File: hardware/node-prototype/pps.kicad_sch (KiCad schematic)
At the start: 5 parts, among them J5 Conn_Coaxial, Q4 2N7002, Q5 AO3401A

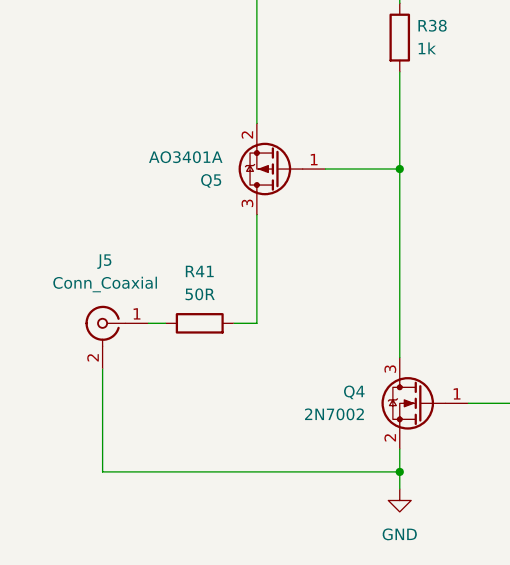
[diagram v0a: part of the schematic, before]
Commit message: Assign footprints
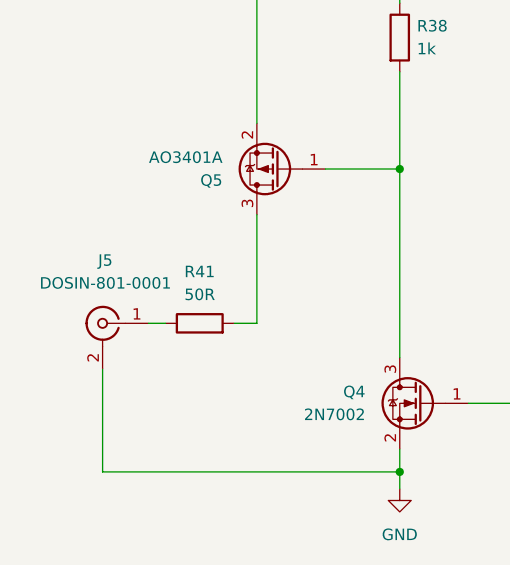
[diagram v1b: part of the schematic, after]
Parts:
- J5: value Conn_Coaxial -> DOSIN-801-0001; footprint (none) -> MYBSP01201ABF_MYBSP00502ABF:DOSIN-801-0001
- R38, R41: footprint (none) -> Resistor_SMD:R_0603_1608Metric
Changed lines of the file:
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@@
       (effects (font (size 1.27 1.27)) (justify left))
     )
-    (property "Footprint" "" (at 160.147 61.595 90)
+    (property "Footprint" "Resistor_SMD:R_0603_1608Metric" (at 160.147 61.595 90)
       (effects (font (size 1.27 1.27)) hide)
     )
@@
       (effects (font (size 1.27 1.27)))
     )
-    (property "Value" "Conn_Coaxial" (at 129.2224 88.9 0)
+    (property "Value" "DOSIN-801-0001" (at 129.2224 88.9 0)
       (effects (font (size 1.27 1.27)))
     )
-    (property "Footprint" "" (at 128.905 93.345 0)
+    (property "Footprint" "MYBSP01201ABF_MYBSP00502ABF:DOSIN-801-0001" (at 128.905 93.345 0)
       (effects (font (size 1.27 1.27)) hide)
     )
-    (property "Datasheet" " ~" (at 128.905 93.345 0)
+    (property "Datasheet" "https://datasheet.lcsc.com/lcsc/2005150732_dosinconn-DOSIN-801-0001_C521212.pdf" (at 128.905 93.345 0)
       (effects (font (size 1.27 1.27)) hide)
     )
@@
       (effects (font (size 1.27 1.27)))
     )
-    (property "Footprint" "" (at 139.7 95.123 90)
+    (property "Footprint" "Resistor_SMD:R_0603_1608Metric" (at 139.7 95.123 90)
       (effects (font (size 1.27 1.27)) hide)
     )

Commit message: Double check schematic
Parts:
- added C35: 1uF, Capacitor_SMD:C_0603_1608Metric, symbol Device:C
- added C47: 100nF, Capacitor_SMD:C_0603_1608Metric, symbol Device:C
- added J6: Conn_01x03, Connector_PinHeader_2.54mm:PinHeader_1x03_P2.54mm_Vertical, symbol Connector_Generic:Conn_01x03
- added JP1: Jumper_2_Open, Jumper:SolderJumper-2_P1.3mm_Open_TrianglePad1.0x1.5mm, symbol Jumper:Jumper_2_Open
- added R47, R51, R52: 100R, Resistor_SMD:R_1206_3216Metric, symbol Device:R
- added R48: 100K, Resistor_SMD:R_0603_1608Metric, symbol Device:R
- added R53: 330K, Resistor_SMD:R_0603_1608Metric, symbol Device:R
- added R54: 47K, Resistor_SMD:R_0603_1608Metric, symbol Device:R
- added R55: 91K, Resistor_SMD:R_0603_1608Metric, symbol Device:R
- added R56: 620K, Resistor_SMD:R_0603_1608Metric, symbol Device:R
- added TP1, TP2 (x2): TestPoint, TestPoint:TestPoint_Pad_D2.0mm, symbol Connector:TestPoint
- added U4: SRV05-4, Package_TO_SOT_SMD:SOT-23-6, symbol Power_Protection:SRV05-4
- R41: value 50R -> 100R; footprint Resistor_SMD:R_0603_1608Metric -> Resistor_SMD:R_1206_3216Metric
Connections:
- net GND: now also C35.2, C47.2, J6.3 (Pin_3), JP1.1 (A), R48.2, R51.1, R52.1, R55.2, R56.2, U4.2 (VN)
- net PPS_OUT: now also TP1.1
- net PPS_BNC: now reaches J5.1 (In), R41.1
- net PPS_BNC: now also R47.1, R48.1, U4.1 (IO1)
- net at Q5.3 (D), R41.2: now also R47.2
- net VDD renamed +5V
- net +5V: now also C35.1, C47.1, U4.5 (VP)
- new net SYNC_IN0: R53.2, R56.1, TP2.1
- new net SYNC_IN1: JP1.2 (B), R54.2, R55.1, TP2.1
- new net SYNC_IN_1M: J6.1 (Pin_1), R53.1, U4.3 (IO2)
- new net SYNC_IN_50R: J6.2 (Pin_2), R51.2, R52.2, R54.1, U4.4 (IO3)
- no-connect marks 0 -> 1
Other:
- moved on the sheet: J5, Q4, Q5, R38, R41

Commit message: Finish placement
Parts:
- added J7: ~, Connector_Coaxial:SMB_Jack_Vertical, symbol Connector:Conn_Coaxial
- J5: value DOSIN-801-0001 -> ~; footprint MYBSP01201ABF_MYBSP00502ABF:DOSIN-801-0001 -> Connector_Coaxial:SMB_Jack_Vertical
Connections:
- net GND: now also J7.2 (Ext)
- net SYNC_IN_50R: now also J7.1 (In)
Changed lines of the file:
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@@
   (junction (at 125.73 58.42) (diameter 0) (color 0 0 0 0)
+  )
+  (junction (at 90.17 109.22) (diameter 0) (color 0 0 0 0)
   )
   (junction (at 110.49 120.65) (diameter 0) (color 0 0 0 0)
@@
     (stroke (width 0) (type default))
   )
+  (wire (pts (xy 78.105 97.155) (xy 78.105 95.885))
+    (stroke (width 0) (type default))
+  )
   (wire (pts (xy 104.14 133.35) (xy 110.49 133.35))
     (stroke (width 0) (type default))
@@
     (stroke (width 0) (type default))
   )
-  (wire (pts (xy 110.49 109.22) (xy 83.82 109.22))
+  (wire (pts (xy 110.49 109.22) (xy 90.17 109.22))
     (stroke (width 0) (type default))
   )
@@
     (stroke (width 0) (type default))
   )
+  (wire (pts (xy 90.17 109.22) (xy 83.82 109.22))
+    (stroke (width 0) (type default))
+  )
   (wire (pts (xy 187.96 36.83) (xy 187.96 34.29))
     (stroke (width 0) (type default))
@@
     (stroke (width 0) (type default))
   )
+  (wire (pts (xy 90.17 90.805) (xy 90.17 109.22))
+    (stroke (width 0) (type default))
+  )
   (wire (pts (xy 63.5 67.31) (xy 67.31 67.31))
     (stroke (width 0) (type default))
@@
   )
   (wire (pts (xy 110.49 120.65) (xy 110.49 123.19))
+    (stroke (width 0) (type default))
+  )
+  (wire (pts (xy 83.185 90.805) (xy 90.17 90.805))
     (stroke (width 0) (type default))
   )
@@
       (effects (font (size 1.27 1.27)))
     )
-    (property "Value" "DOSIN-801-0001" (at 58.7374 62.865 0)
-      (effects (font (size 1.27 1.27)))
-    )
-    (property "Footprint" "MYBSP01201ABF_MYBSP00502ABF:DOSIN-801-0001" (at 58.42 67.31 0)
+    (property "Value" "~" (at 58.7374 62.865 0)
+      (effects (font (size 1.27 1.27)))
+    )
+    (property "Footprint" "Connector_Coaxial:SMB_Jack_Vertical" (at 58.42 67.31 0)
       (effects (font (size 1.27 1.27)) hide)
     )
@@
     )
   )
+  (symbol (lib_id "Connector:Conn_Coaxial") (at 78.105 90.805 0) (mirror y) (unit 1)
+    (in_bom yes) (on_board yes) (dnp no) (fields_autoplaced)
+    (property "Reference" "J7" (at 78.4224 83.82 0)
+      (effects (font (size 1.27 1.27)))
+    )
+    (property "Value" "~" (at 78.4224 86.36 0)
+      (effects (font (size 1.27 1.27)))
+    )
+    (property "Footprint" "Connector_Coaxial:SMB_Jack_Vertical" (at 78.105 90.805 0)
+      (effects (font (size 1.27 1.27)) hide)
+    )
+    (property "Datasheet" " ~" (at 78.105 90.805 0)
+      (effects (font (size 1.27 1.27)) hide)
+    )
+    (pin "1")
+    (pin "2")
+    (instances
+      (project "node-prototype"
+        (path "/294f7425-8100-4c88-a430-3b04b29ed98a/34bb779a-dbcb-4b81-a840-258e700bb8f3"
+          (reference "J7") (unit 1)
+        )
+      )
+    )
+  )
   (symbol (lib_id "Connector:TestPoint") (at 116.205 120.65 0) (unit 1)
     (in_bom yes) (on_board yes) (dnp no) (fields_autoplaced)
@@
         )
       )
+    )
+  )
+  (symbol (lib_id "power:GND") (at 78.105 97.155 0) (unit 1)
+    (in_bom yes) (on_board yes) (dnp no) (fields_autoplaced)
+    (property "Reference" "#PWR0106" (at 78.105 103.505 0)
+      (effects (font (size 1.27 1.27)) hide)
+    )
+    (property "Value" "GND" (at 78.105 102.235 0)
+      (effects (font (size 1.27 1.27)))
+    )
+    (property "Footprint" "" (at 78.105 97.155 0)
+      (effects (font (size 1.27 1.27)) hide)
+    )
+    (property "Datasheet" "" (at 78.105 97.155 0)
+      (effects (font (size 1.27 1.27)) hide)
+    )
+    (pin "1")
+    (instances
+      (project "node-prototype"
+        (path "/294f7425-8100-4c88-a430-3b04b29ed98a/34bb779a-dbcb-4b81-a840-258e700bb8f3"
+          (reference "#PWR0106") (unit 1)
+        )
+      )

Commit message: prepare for production
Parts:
- J5, J6, J7: now not fitted
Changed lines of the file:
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@@
   )
   (symbol (lib_id "Connector:Conn_Coaxial") (at 58.42 67.31 0) (mirror y) (unit 1)
-    (in_bom yes) (on_board yes) (dnp no) (fields_autoplaced)
+    (in_bom yes) (on_board yes) (dnp yes) (fields_autoplaced)
     (property "Reference" "J5" (at 58.7374 60.325 0)
       (effects (font (size 1.27 1.27)))
@@
   )
   (symbol (lib_id "Connector_Generic:Conn_01x03") (at 58.42 109.22 0) (mirror y) (unit 1)
-    (in_bom yes) (on_board yes) (dnp no) (fields_autoplaced)
+    (in_bom yes) (on_board yes) (dnp yes) (fields_autoplaced)
     (property "Reference" "J6" (at 58.42 100.33 0)
       (effects (font (size 1.27 1.27)))
@@
   )
   (symbol (lib_id "Connector:Conn_Coaxial") (at 78.105 90.805 0) (mirror y) (unit 1)
-    (in_bom yes) (on_board yes) (dnp no) (fields_autoplaced)
+    (in_bom yes) (on_board yes) (dnp yes) (fields_autoplaced)
     (property "Reference" "J7" (at 78.4224 83.82 0)
       (effects (font (size 1.27 1.27)))
